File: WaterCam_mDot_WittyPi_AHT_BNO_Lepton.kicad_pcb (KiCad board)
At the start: 2 copper layers, 116.3 x 65.3 mm, 12 parts, among them J1 GPIO, J2 FLIR Lepton, P3 Witty Pi 4 P3, Q1 NMOS, U1 ATH20, U2 BNO055 IMU, U3 MDOT

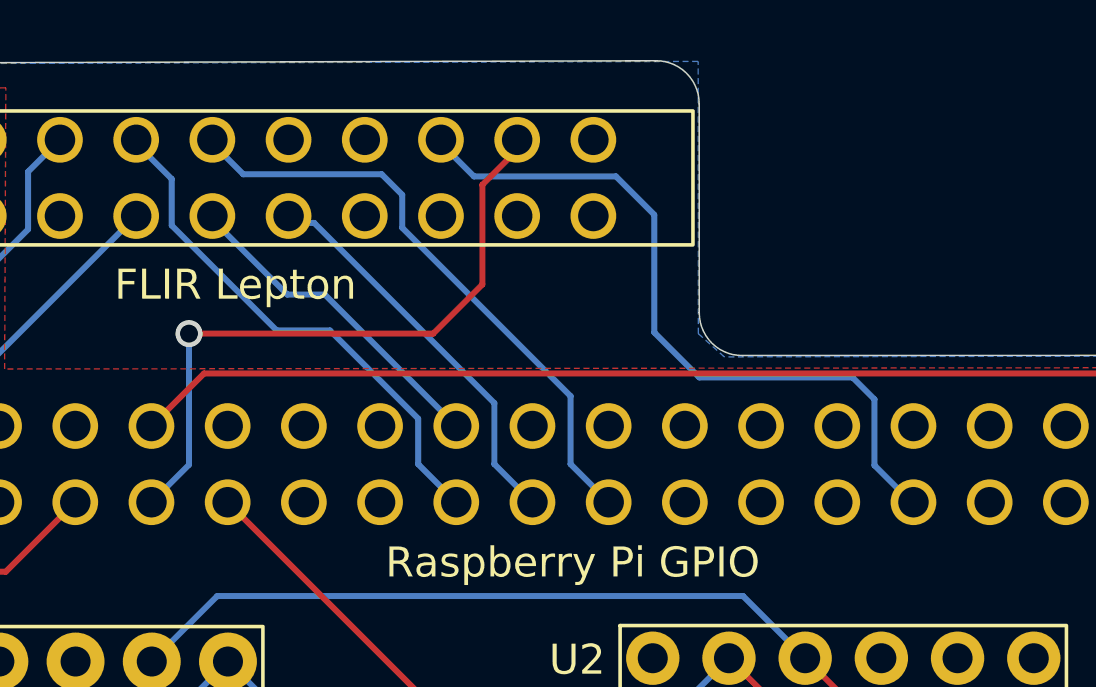
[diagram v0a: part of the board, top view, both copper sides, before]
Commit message: Fix GPIO17, MASTER_CLK, WittyPi SW short, Q1 mis-pinning; OSHPark rules
Rebased onto main after #1 (schematic corrections). The schematic and board
are this commit's versions: they build on #1's corrections and deliberately
drop U4/R4/R5 (HAT EEPROM not needed; overlays load from config.txt) and J4
(the IR-cut circuit is deferred as external to the HAT), as recorded in
WaterCam_PCB_Design_Changes_Required.md.

Left out of the public repo: KiCad auto-backup zips, autosave/lock/-bak
files, per-user .kicad_prl and .history, and the vendor datasheets and
manuals (References/README.md lists where to get them). .gitignore keeps
them out.

Co-Authored-By: Claude Opus 5.5 <noreply@anthropic.com>
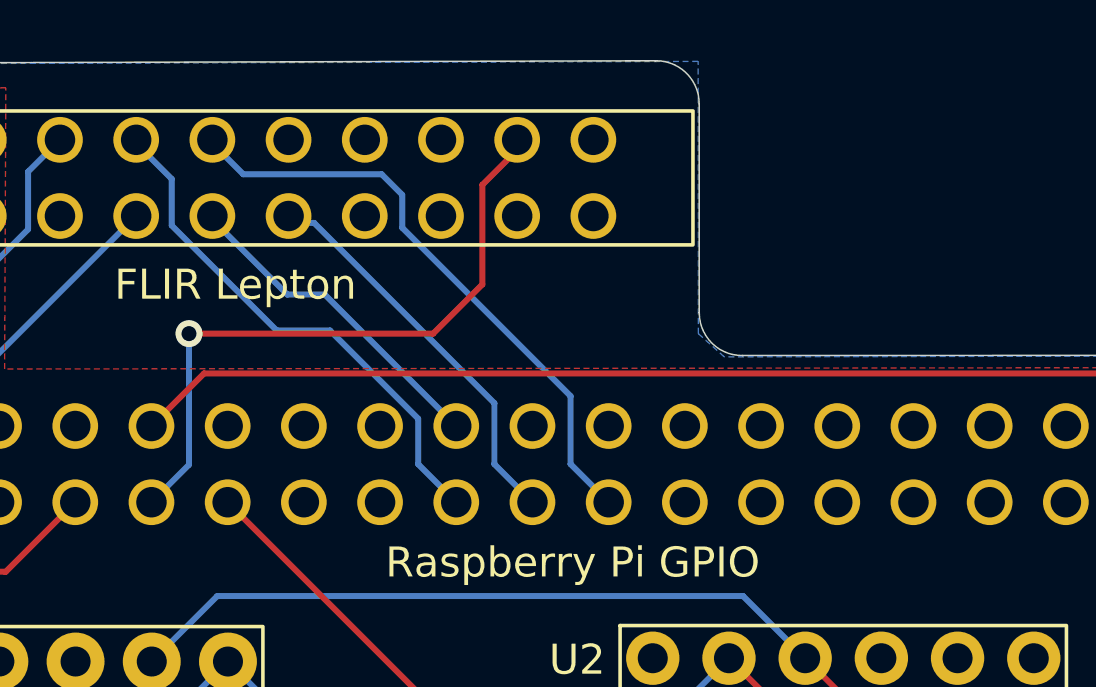
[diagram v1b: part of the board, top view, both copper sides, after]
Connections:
- J1 pad 11: /GPIO17 -> (no net)
- J2 pad 15: /GPIO17 -> (no net)
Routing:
- net /GPIO17: track 24.8 -> 0.00 mm

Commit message: v6 work in progress: BNO055 fixes, sensor rails, placement (not yet routed)
Checkpoint of the 2026-09-09 session on top of the OSHPark-rules commit:
- Schematic: BNO055 fixes, sensor power rails, U2 INT no-connect.
- PCB: F8, component placement and fixes from that session; all 22
  footprints on the board, 0 shorts and 0 solder-mask bridges (were 8/8).
- SESSION_HANDOFF.md: status, the remaining DRC items, routing order,
  open assembly decisions, and two risks to check before ordering (BNO055
  pad 1 has no orientation marking; MDOT footprint duplicates pad 24).

Not orderable: 26 connections unrouted, 17 DRC violations.

tools/kicad_pin_positions.py and tools/pdf_vector_extract.py are the
session's helper scripts turned into small CLI tools (paths are arguments).

Co-Authored-By: Claude Opus 5.5 <noreply@anthropic.com>
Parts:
- added C1: 100µF, Capacitor_SMD:C_0805_2012Metric, F.Cu at (132.1, 55.0)
- added C2: 100nF, Capacitor_SMD:C_0402_1005Metric, F.Cu at (125.5, 54.5)
- added C3: 100nF, Capacitor_SMD:C_0402_1005Metric, F.Cu at (65.0, 65.5)
- added C4: 10µF, Capacitor_SMD:C_0402_1005Metric, F.Cu at (65.0, 67.5)
- added C5: 100nF, Capacitor_SMD:C_0402_1005Metric, F.Cu at (95.0, 65.0)
- added C6: 100nF, Capacitor_SMD:C_0402_1005Metric, F.Cu at (55.5, 41.5)
- added R6: 4.7kΩ, Resistor_SMD:R_0402_1005Metric, F.Cu at (78.0, 63.0)
- added R7: 4.7kΩ, Resistor_SMD:R_0402_1005Metric, F.Cu at (78.0, 65.0)
- added R8: 100Ω, Resistor_SMD:R_0402_1005Metric, F.Cu at (132.5, 63.0)
- added R9: 10kΩ, Resistor_SMD:R_0402_1005Metric, F.Cu at (133.0, 70.0)
- J2: value FLIR Lepton -> FLIR Lepton Socket
- J3: renamed from P3; value Witty Pi 4 P3 -> Witty Pi 4 L3V7 P3 Header
- Q1: value NMOS -> BSS138; footprint IRLB8721PBF Model:TO254P1067X483X2057-3 -> Package_TO_SOT_SMD:SOT-23
- U2: value BNO055 IMU -> BNO055(IMU)
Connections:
- net Net-(J3-3V3) renamed /WP_3V3
- J1 pad 1: unconnected-(J1-Pin_1-Pad1) -> +3V3
- J1 pad 11: (no net) -> unconnected-(J1-Pin_11-Pad11)
- J1 pad 27: /ID_SDA -> unconnected-(J1-Pin_27-Pad27)
- J1 pad 28: /ID_SCL -> unconnected-(J1-Pin_28-Pad28)
- J2 pad 15: (no net) -> unconnected-(J2-Pin_15-Pad15)
- J3 pad 5: Net-(J3-SW) -> /WP_SW
- Q1 pad 1: Net-(J3-SW) -> Net-(Q1-G)
- Q1 pad 2: Net-(Q1-G) -> GND
- Q1 pad 3: GND -> /WP_SW
- R3 pad 2: Net-(Q1-G) -> Net-(U3-PB_1)
- U1 pad 1: +5V -> +3V3
- U2 pad 1: unconnected-(U2-RST-Pad1) -> /GPIO16
- U2 pad 6: +5V -> +3V3
- U3 pad 19: Net-(Q1-G) -> Net-(U3-PB_1)
- U3 pad 5: unconnected-(U3-NRESET-Pad5) -> Net-(U3-NRESET)
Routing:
- net Net-(Q1-G): track 78.6 -> 0.00 mm
- net Net-(J3-SW): track 39.3 -> 0.00 mm
- net /WP_SW: track 0.00 -> 39.3 mm
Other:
- board text added: "AHT20 Header"
- board text removed: "BNO055 IMU Header"
